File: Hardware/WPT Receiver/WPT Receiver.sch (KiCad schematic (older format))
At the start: 157 parts, among them J1 0.1\" Header, J2 Tag-connect-NL, J3 0.1\" Header, J4 0.1\" Header, SW1 PTS647, SW2 PTS647, SW3 PTS647, U1 STM32G031C6U6, U10 74HC595, U2 INA180A3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

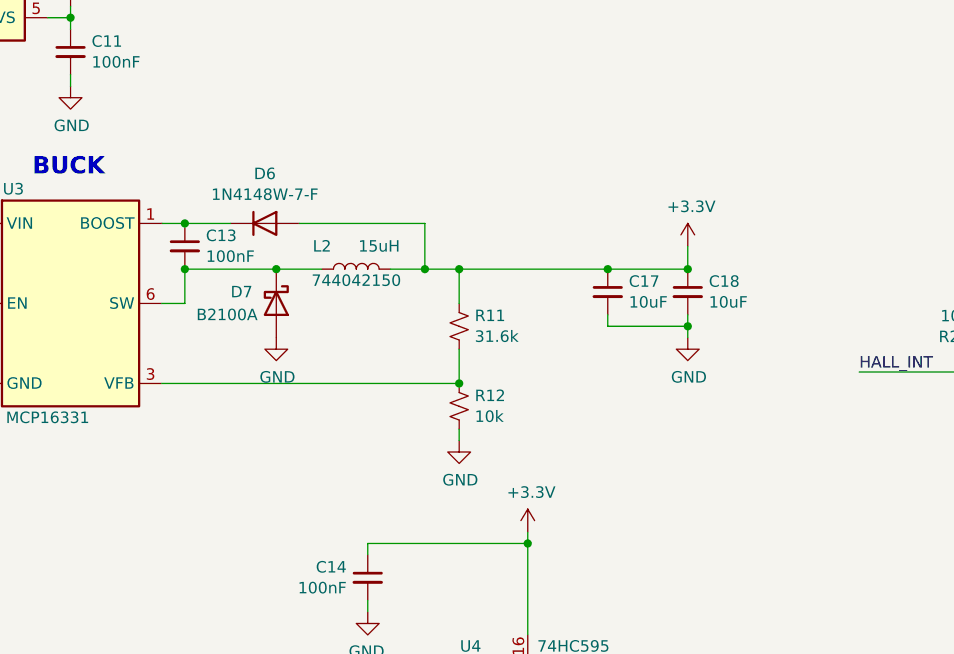
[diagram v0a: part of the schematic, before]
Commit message: Added routing for power input region (including buck) and a few other remaining signals. All signals now routed other than ground
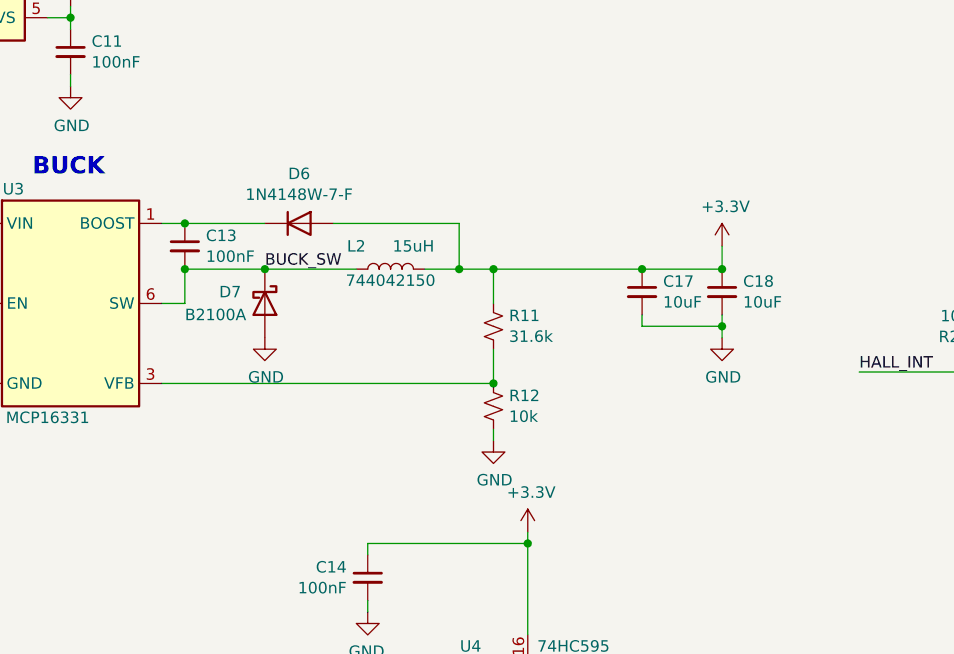
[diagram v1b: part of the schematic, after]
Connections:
- net BUCK_SW: now reaches C13.2, D7.1 (K), L2.1, U3.6 (SW)
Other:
- moved on the sheet: C17, C18, D6, D7, L2, R11, R12
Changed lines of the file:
@@
 L WPT_Project_Parts:1N4148W-7-F D6
 U 1 1 60AC2E91
-P 5150 3100
-F 0 "D6" H 5150 3317 50  0000 C CNN
-F 1 "1N4148W-7-F" H 5150 3226 50  0000 C CNN
-F 2 "Diode_SMD:D_SOD-123" H 5150 2925 50  0001 C CNN
-F 3 "https://www.diodes.com/assets/Datasheets/ds30086.pdf" H 5150 3100 50  0001 C CNN
-	1    5150 3100
+P 5300 3100
+F 0 "D6" H 5300 3317 50  0000 C CNN
+F 1 "1N4148W-7-F" H 5300 3226 50  0000 C CNN
+F 2 "Diode_SMD:D_SOD-123" H 5300 2925 50  0001 C CNN
+F 3 "https://www.diodes.com/assets/Datasheets/ds30086.pdf" H 5300 3100 50  0001 C CNN
+	1    5300 3100
 	1    0    0    -1
 $EndComp
@@
 L WPT_Project_Parts:B2100A D7
 U 1 1 60AC340A
-P 5200 3450
-F 0 "D7" V 5150 3250 50  0000 L CNN
-F 1 "B2100A" V 5250 3100 50  0000 L CNN
-F 2 "Diode_SMD:D_SMA" H 5200 3275 50  0001 C CNN
-F 3 "https://www.diodes.com/assets/Datasheets/B2100A.pdf" H 5200 3450 50  0001 C CNN
-	1    5200 3450
+P 5150 3450
+F 0 "D7" V 5100 3250 50  0000 L CNN
+F 1 "B2100A" V 5200 3100 50  0000 L CNN
+F 2 "Diode_SMD:D_SMA" H 5150 3275 50  0001 C CNN
+F 3 "https://www.diodes.com/assets/Datasheets/B2100A.pdf" H 5150 3450 50  0001 C CNN
+	1    5150 3450
 	0    1    1    0
 $EndComp
@@
 L Device:L L2
 U 1 1 60AC40EF
-P 5550 3300
-F 0 "L2" V 5650 3450 50  0000 C CNN
-F 1 "15uH" V 5650 3200 50  0000 C CNN
-F 2 "WPT_Project_Parts:744042150" H 5550 3300 50  0001 C CNN
-F 3 "https://www.we-online.de/katalog/datasheet/744042150.pdf" H 5550 3300 50  0001 C CNN
-F 4 "744042150" V 5500 3300 50  0000 C CNN "MPN"
-	1    5550 3300
+P 5700 3300
+F 0 "L2" V 5800 3450 50  0000 C CNN
+F 1 "15uH" V 5800 3200 50  0000 C CNN
+F 2 "WPT_Project_Parts:744042150" H 5700 3300 50  0001 C CNN
+F 3 "https://www.we-online.de/katalog/datasheet/744042150.pdf" H 5700 3300 50  0001 C CNN
+F 4 "744042150" V 5650 3300 50  0000 C CNN "MPN"
+	1    5700 3300
 	0    -1   -1   0
 $EndComp
@@
 L Device:R_Small_US R11
 U 1 1 60AC4794
-P 6000 3550
-F 0 "R11" H 6068 3596 50  0000 L CNN
-F 1 "31.6k" H 6068 3505 50  0000 L CNN
-F 2 "Resistor_SMD:R_0603_1608Metric" H 6000 3550 50  0001 C CNN
-F 3 "~" H 6000 3550 50  0001 C CNN
-	1    6000 3550
+P 6150 3550
+F 0 "R11" H 6218 3596 50  0000 L CNN
+F 1 "31.6k" H 6218 3505 50  0000 L CNN
+F 2 "Resistor_SMD:R_0603_1608Metric" H 6150 3550 50  0001 C CNN
+F 3 "~" H 6150 3550 50  0001 C CNN
+	1    6150 3550
 	1    0    0    -1
 $EndComp
@@
 L Device:R_Small_US R12
 U 1 1 60AC4E53
-P 6000 3900
-F 0 "R12" H 6068 3946 50  0000 L CNN
-F 1 "10k" H 6068 3855 50  0000 L CNN
-F 2 "Resistor_SMD:R_0603_1608Metric" H 6000 3900 50  0001 C CNN
-F 3 "~" H 6000 3900 50  0001 C CNN
-	1    6000 3900
+P 6150 3900
+F 0 "R12" H 6218 3946 50  0000 L CNN
+F 1 "10k" H 6218 3855 50  0000 L CNN
+F 2 "Resistor_SMD:R_0603_1608Metric" H 6150 3900 50  0001 C CNN
+F 3 "~" H 6150 3900 50  0001 C CNN
+	1    6150 3900
 	1    0    0    -1
 $EndComp
@@
 L Device:C_Small C17
 U 1 1 60AC5C99
-P 6650 3400
-F 0 "C17" H 6742 3446 50  0000 L CNN
-F 1 "10uF" H 6742 3355 50  0000 L CNN
-F 2 "Capacitor_SMD:C_0603_1608Metric" H 6650 3400 50  0001 C CNN
-F 3 "~" H 6650 3400 50  0001 C CNN
-	1    6650 3400
+P 6800 3400
+F 0 "C17" H 6892 3446 50  0000 L CNN
+F 1 "10uF" H 6892 3355 50  0000 L CNN
+F 2 "Capacitor_SMD:C_0603_1608Metric" H 6800 3400 50  0001 C CNN
+F 3 "~" H 6800 3400 50  0001 C CNN
+	1    6800 3400
 	1    0    0    -1
 $EndComp
@@
 L Device:C_Small C18
 U 1 1 60AC63AF
-P 7000 3400
-F 0 "C18" H 7092 3446 50  0000 L CNN
-F 1 "10uF" H 7092 3355 50  0000 L CNN
-F 2 "Capacitor_SMD:C_0603_1608Metric" H 7000 3400 50  0001 C CNN
-F 3 "~" H 7000 3400 50  0001 C CNN
-	1    7000 3400
+P 7150 3400
+F 0 "C18" H 7242 3446 50  0000 L CNN
+F 1 "10uF" H 7242 3355 50  0000 L CNN
+F 2 "Capacitor_SMD:C_0603_1608Metric" H 7150 3400 50  0001 C CNN
+F 3 "~" H 7150 3400 50  0001 C CNN
+	1    7150 3400
 	1    0    0    -1
 $EndComp
@@
 	4700 3100 4800 3100
 Wire Wire Line
-	4800 3100 5000 3100
+	4800 3100 5150 3100
 Connection ~ 4800 3100
 Wire Wire Line
@@
 	4800 3450 4800 3300
 Wire Wire Line
-	4800 3300 5200 3300
+	4800 3300 5150 3300
 Connection ~ 4800 3300
 $Comp
 L power:GND #PWR028
 U 1 1 60AE11A4
-P 5200 3600
-F 0 "#PWR028" H 5200 3350 50  0001 C CNN
-F 1 "GND" H 5205 3427 50  0000 C CNN
-F 2 "" H 5200 3600 50  0001 C CNN
-F 3 "" H 5200 3600 50  0001 C CNN
-	1    5200 3600
+P 5150 3600
+F 0 "#PWR028" H 5150 3350 50  0001 C CNN
+F 1 "GND" H 5155 3427 50  0000 C CNN
+F 2 "" H 5150 3600 50  0001 C CNN
+F 3 "" H 5150 3600 50  0001 C CNN
+	1    5150 3600
 	1    0    0    -1
 $EndComp
-Connection ~ 5200 3300
+Connection ~ 5150 3300
 Wire Wire Line
-	5200 3300 5400 3300
+	5150 3300 5550 3300
 Wire Wire Line
-	5700 3300 5850 3300
+	5850 3300 6000 3300
 Wire Wire Line
-	5300 3100 5850 3100
+	5450 3100 6000 3100
 Wire Wire Line
-	5850 3100 5850 3300
-Connection ~ 5850 3300
+	6000 3100 6000 3300
+Connection ~ 6000 3300
 Wire Wire Line
-	4700 3800 6000 3800
+	4700 3800 6150 3800
 Wire Wire Line
-	6000 3800 6000 3650
+	6150 3800 6150 3650
 Wire Wire Line
-	5850 3300 6000 3300
-Connection ~ 6000 3800
+	6000 3300 6150 3300
+Connection ~ 6150 3800
 Wire Wire Line
-	6000 3450 6000 3300
-Connection ~ 6000 3300
+	6150 3450 6150 3300
+Connection ~ 6150 3300
 $Comp
 L power:GND #PWR031
 U 1 1 60AE5155
-P 6000 4050
-F 0 "#PWR031" H 6000 3800 50  0001 C CNN
-F 1 "GND" H 6005 3877 50  0000 C CNN
-F 2 "" H 6000 4050 50  0001 C CNN
-F 3 "" H 6000 4050 50  0001 C CNN
-	1    6000 4050
+P 6150 4050
+F 0 "#PWR031" H 6150 3800 50  0001 C CNN
+F 1 "GND" H 6155 3877 50  0000 C CNN
+F 2 "" H 6150 4050 50  0001 C CNN
+F 3 "" H 6150 4050 50  0001 C CNN
+	1    6150 4050
 	1    0    0    -1
 $EndComp
 Wire Wire Line
-	6000 4050 6000 4000
+	6150 4050 6150 4000
 Wire Wire Line
 	3900 3450 3750 3450
@@
 L power:GND #PWR041
 U 1 1 60AEADEB
-P 7000 3600
-F 0 "#PWR041" H 7000 3350 50  0001 C CNN
-F 1 "GND" H 7005 3427 50  0000 C CNN
-F 2 "" H 7000 3600 50  0001 C CNN
-F 3 "" H 7000 3600 50  0001 C CNN
-	1    7000 3600
+P 7150 3600
+F 0 "#PWR041" H 7150 3350 50  0001 C CNN
+F 1 "GND" H 7155 3427 50  0000 C CNN
+F 2 "" H 7150 3600 50  0001 C CNN
+F 3 "" H 7150 3600 50  0001 C CNN
+	1    7150 3600
 	1    0    0    -1
 $EndComp
 Wire Wire Line
-	6000 3300 6650 3300
-Connection ~ 6650 3300
+	6150 3300 6800 3300
+Connection ~ 6800 3300
 Wire Wire Line
-	6650 3300 7000 3300
+	6800 3300 7150 3300
 Wire Wire Line
-	6650 3500 6650 3550
+	6800 3500 6800 3550
 Wire Wire Line
-	6650 3550 7000 3550
+	6800 3550 7150 3550
 Wire Wire Line
-	7000 3550 7000 3500
+	7150 3550 7150 3500
 Wire Wire Line
-	7000 3600 7000 3550
-Connection ~ 7000 3550
+	7150 3600 7150 3550
+Connection ~ 7150 3550
 $Comp
 L power:+3.3V #PWR040
 U 1 1 60AED472
-P 7000 3200
-F 0 "#PWR040" H 7000 3050 50  0001 C CNN
-F 1 "+3.3V" H 7015 3373 50  0000 C CNN
-F 2 "" H 7000 3200 50  0001 C CNN
-F 3 "" H 7000 3200 50  0001 C CNN
-	1    7000 3200
+P 7150 3200
+F 0 "#PWR040" H 7150 3050 50  0001 C CNN
+F 1 "+3.3V" H 7165 3373 50  0000 C CNN
+F 2 "" H 7150 3200 50  0001 C CNN
+F 3 "" H 7150 3200 50  0001 C CNN
+	1    7150 3200
 	1    0    0    -1
 $EndComp
 Wire Wire Line
-	7000 3300 7000 3200
-Connection ~ 7000 3300
+	7150 3300 7150 3200
+Connection ~ 7150 3300
 $Comp
 L WPT_Project_Parts:STM32G031C6U6 U1
@@
 	3600 8100 4100 8100
 NoConn ~ 3600 5200
+Text Label 5150 3300 0    50   ~ 0
+BUCK_SW
 $EndSCHEMATC
